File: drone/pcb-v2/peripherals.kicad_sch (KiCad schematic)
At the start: 22 parts, among them J2 Conn_02x11_Odd_Even, J4 Conn_01x04_MountingPin, SW1 SW_Push, SW3 SW_Push, U1 MPU6500, U5 NRF24L01_Breakout, U8 HYCW110-TF10-180B

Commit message: [pcb] schematic v2: footprint/part assignments
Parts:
- C5: renamed from C32; now left out of the parts list
- C6: renamed from C3; footprint Capacitor_SMD:C_0805_2012Metric_Pad1.18x1.45mm_HandSolder -> Capacitor_SMD:C_0603_1608Metric
- C7: renamed from C2; footprint Capacitor_SMD:C_0805_2012Metric_Pad1.18x1.45mm_HandSolder -> Capacitor_SMD:C_0603_1608Metric; LCSC (none) -> C14663
- C8: renamed from C1; footprint Capacitor_SMD:C_0805_2012Metric_Pad1.18x1.45mm_HandSolder -> Capacitor_SMD:C_0603_1608Metric; LCSC (none) -> C14663
- D5: renamed from D7; now left out of the parts list
- D6: renamed from D8; now left out of the parts list
- D7: renamed from D5; now left out of the parts list
- D8: renamed from D6; now left out of the parts list
- J1: renamed from J4; now left out of the parts list
- J2, SW1: now left out of the parts list
- R10: renamed from R23; now left out of the parts list
- R11: renamed from R21; now left out of the parts list
- R12: renamed from R20; now left out of the parts list
- R13: renamed from R22; footprint Resistor_SMD:R_0805_2012Metric -> Resistor_SMD:R_0805_2012Metric_Pad1.20x1.40mm_HandSolder; now left out of the parts list
- R14: renamed from R25; footprint Resistor_SMD:R_0805_2012Metric -> Resistor_SMD:R_0805_2012Metric_Pad1.20x1.40mm_HandSolder; now left out of the parts list
- R9: renamed from R24; now left out of the parts list
- SW2: renamed from SW3; now left out of the parts list
- U1: renamed from U5; now left out of the parts list
- U2: renamed from U8; now left out of the parts list
- renumbered JP2 to JP1, U1 to U3

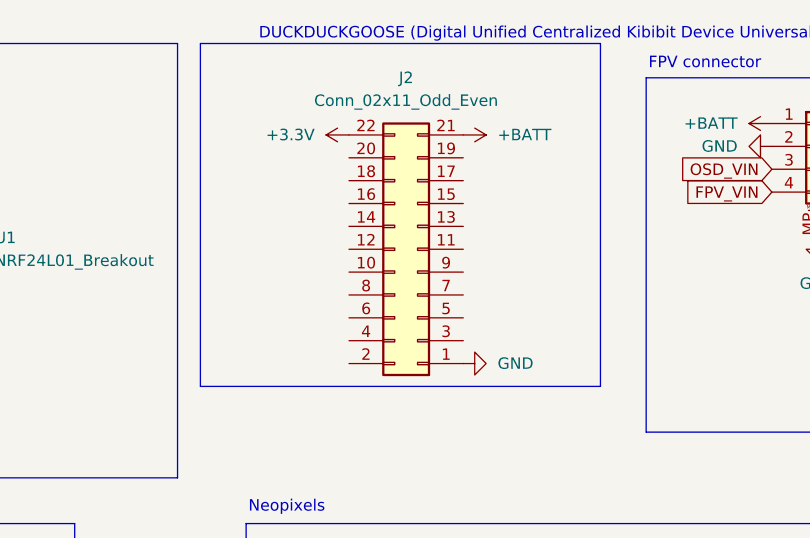
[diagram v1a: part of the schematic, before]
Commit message: [pcb] pcb v2: component placement
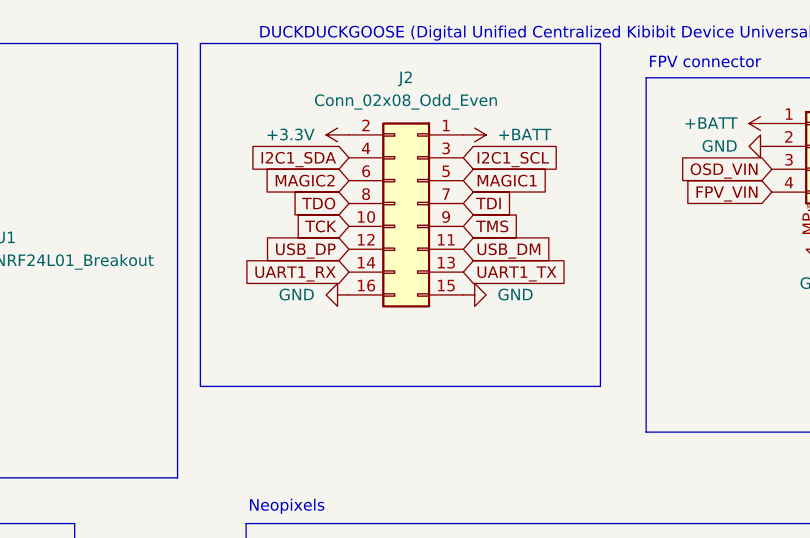
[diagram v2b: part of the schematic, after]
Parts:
- removed J2: Conn_02x11_Odd_Even, Connector_PinHeader_2.54mm:PinHeader_2x11_P2.54mm_Vertical, symbol Connector_Generic:Conn_02x11_Odd_Even
- added J2: Conn_02x08_Odd_Even, Connector_PinHeader_2.54mm:PinHeader_2x08_P2.54mm_Vertical, symbol Connector_Generic:Conn_02x08_Odd_Even
- R10, R11, R12, R9: footprint Resistor_SMD:R_0805_2012Metric_Pad1.20x1.40mm_HandSolder -> Resistor_SMD:R_0805_2012Metric; LCSC (none) -> C17414; now in the parts list
- U3: footprint lcsc:QFN-24_L3.0-W3.0-P0.40-BL-EP -> Package_DFN_QFN:QFN-24-1EP_3x3mm_P0.4mm_EP1.75x1.6mm
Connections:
- net +3.3V: now also J2.2 (Pin_2)
- net +BATT: now also J2.1 (Pin_1)
- net GND: now also J2.15 (Pin_15), J2.16 (Pin_16)
- new net I2C1_SCL: J2.3 (Pin_3)
- new net I2C1_SDA: J2.4 (Pin_4)
- new net MAGIC1: J2.5 (Pin_5)
- new net MAGIC2: J2.6 (Pin_6)
- new net TCK: J2.10 (Pin_10)
- new net TDI: J2.7 (Pin_7)
- new net TDO: J2.8 (Pin_8)
- new net TMS: J2.9 (Pin_9)
- new net UART1_RX: J2.14 (Pin_14)
- new net UART1_TX: J2.13 (Pin_13)
- new net USB_DM: J2.11 (Pin_11)
- new net USB_DP: J2.12 (Pin_12)

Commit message: [pcb] finish routing
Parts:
- removed SW2: SW_Push, lcsc:SW-SMD_L4.0-W2.9-LS5.0, symbol Switch:SW_Push
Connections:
- net SD_CS: no longer U2.9 (CD)
- net SPI1_CLK: no longer U1.5 (SCK)
- net SPI1_MISO: no longer U1.7 (MISO)
- net SPI1_MOSI: no longer U1.6 (MOSI)
- net TCK: now also J2.9 (Pin_9); no longer J2.10 (Pin_10)
- net TMS: now also J2.10 (Pin_10); no longer J2.9 (Pin_9)
- net USB_DM renamed D-
- net USB_DP renamed D+
- new net SD_CD: U2.9 (CD)
- new net SPI2_CLK: U1.5 (SCK)
- new net SPI2_MISO: U1.7 (MISO)
- new net SPI2_MOSI: U1.6 (MOSI)
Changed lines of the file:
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@@
 	(rectangle
 		(start 19.05 69.85)
-		(end 64.77 93.98)
+		(end 40.64 93.98)
 		(stroke
 			(width 0)
@@
 		)
 	)
-	(global_label "SPI1_MOSI"
+	(global_label "SPI2_MOSI"
 		(shape input)
 		(at 33.02 31.75 180)
@@
 		)
 	)
-	(global_label "USB_DP"
+	(global_label "D-"
 		(shape input)
-		(at 95.25 39.37 180)
+		(at 107.95 39.37 0)
 		(fields_autoplaced yes)
 		(effects
@@
 				(size 1.27 1.27)
 			)
-			(justify right)
+			(justify left)
 		)
 		(property "Intersheetrefs" "${INTERSHEET_REFS}"
-			(at 84.9472 39.37 0)
+			(at 113.7776 39.37 0)
 			(effects
 				(font
 					(size 1.27 1.27)
 				)
-				(justify right)
+				(justify left)
 				(hide yes)
 			)
@@
 		)
 	)
-	(global_label "BTN2"
+	(global_label "IMU_INT1"
 		(shape input)
-		(at 54.61 85.09 0)
+		(at 41.91 137.16 180)
 		(fields_autoplaced yes)
 		(effects
@@
 				(size 1.27 1.27)
 			)
-			(justify left)
+			(justify right)
 		)
 		(property "Intersheetrefs" "${INTERSHEET_REFS}"
-			(at 62.3728 85.09 0)
+			(at 30.4581 137.16 0)
 			(effects
 				(font
 					(size 1.27 1.27)
 				)
-				(justify left)
+				(justify right)
 				(hide yes)
 			)
 		)
 	)
-	(global_label "TMS"
+	(global_label "BTN1"
 		(shape input)
-		(at 107.95 36.83 0)
+		(at 31.75 85.09 0)
 		(fields_autoplaced yes)
 		(effects
@@
 		)
 		(property "Intersheetrefs" "${INTERSHEET_REFS}"
-			(at 114.5637 36.83 0)
+			(at 39.5128 85.09 0)
 			(effects
 				(font
@@
 		)
 	)
-	(global_label "IMU_INT1"
+	(global_label "SPI1_CLK"
 		(shape input)
-		(at 41.91 137.16 180)
+		(at 236.22 49.53 180)
 		(fields_autoplaced yes)
 		(effects
@@
 		)
 		(property "Intersheetrefs" "${INTERSHEET_REFS}"
-			(at 30.4581 137.16 0)
+			(at 224.4053 49.53 0)
 			(effects
 				(font
@@
 		)
 	)
-	(global_label "BTN1"
-		(shape input)
-		(at 31.75 85.09 0)
-		(fields_autoplaced yes)
-		(effects
-			(font
-				(size 1.27 1.27)
-			)
-			(justify left)
-		)
-		(property "Intersheetrefs" "${INTERSHEET_REFS}"
-			(at 39.5128 85.09 0)
-			(effects
-				(font
-					(size 1.27 1.27)
-				)
-				(justify left)
-				(hide yes)
-			)
-		)
-	)
-	(global_label "SPI1_CLK"
+	(global_label "MAGIC2"
 		(shape input)
-		(at 236.22 49.53 180)
+		(at 95.25 31.75 180)
 		(fields_autoplaced yes)
 		(effects
@@
 		)
 		(property "Intersheetrefs" "${INTERSHEET_REFS}"
-			(at 224.4053 49.53 0)
+			(at 85.3705 31.75 0)
 			(effects
 				(font
@@
 		)
 	)
-	(global_label "USB_DM"
+	(global_label "STATUS_LED_2"
 		(shape input)
-		(at 107.95 39.37 0)
+		(at 190.5 116.84 0)
 		(fields_autoplaced yes)
 		(effects
@@
 		)
 		(property "Intersheetrefs" "${INTERSHEET_REFS}"
-			(at 118.4342 39.37 0)
+			(at 206.8503 116.84 0)
 			(effects
 				(font
@@
 		)
 	)
-	(global_label "MAGIC2"
+	(global_label "TCK"
 		(shape input)
-		(at 95.25 31.75 180)
+		(at 107.95 36.83 0)
 		(fields_autoplaced yes)
 		(effects
@@
 				(size 1.27 1.27)
 			)
-			(justify right)
+			(justify left)
 		)
 		(property "Intersheetrefs" "${INTERSHEET_REFS}"
-			(at 85.3705 31.75 0)
+			(at 114.4428 36.83 0)
 			(effects
 				(font
 					(size 1.27 1.27)
 				)
-				(justify right)
+				(justify left)
 				(hide yes)
 			)
 		)
 	)
-	(global_label "STATUS_LED_2"
+	(global_label "D+"
 		(shape input)
-		(at 190.5 116.84 0)
+		(at 95.25 39.37 180)
 		(fields_autoplaced yes)
 		(effects
@@
 				(size 1.27 1.27)
 			)
-			(justify left)
+			(justify right)
 		)
 		(property "Intersheetrefs" "${INTERSHEET_REFS}"
-			(at 206.8503 116.84 0)
+			(at 89.4224 39.37 0)
 			(effects
 				(font
 					(size 1.27 1.27)
 				)
-				(justify left)
+				(justify right)
 				(hide yes)
 			)
@@
 		)
 	)
-	(global_label "SPI1_CLK"
+	(global_label "SPI2_CLK"
 		(shape input)
 		(at 33.02 36.83 180)
@@
 		)
 	)
-	(global_label "SPI1_MISO"
+	(global_label "SPI2_MISO"
 		(shape input)
 		(at 33.02 34.29 180)
@@
 		)
 	)
-	(global_label "SPI1_MISO"
+	(global_label "TMS"
 		(shape input)
-		(at 41.91 129.54 180)
+		(at 95.25 36.83 180)
 		(fields_autoplaced yes)
 		(effects
@@
 		)
 		(property "Intersheetrefs" "${INTERSHEET_REFS}"
-			(at 29.0672 129.54 0)
+			(at 88.6363 36.83 0)
 			(effects
 				(font
@@
 		)
 	)
-	(global_label "SD_CS"
+	(global_label "SPI1_MISO"
 		(shape input)
-		(at 256.54 44.45 0)
+		(at 41.91 129.54 180)
 		(fields_autoplaced yes)
 		(effects
@@
 				(size 1.27 1.27)
 			)
-			(justify left)
+			(justify right)
 		)
 		(property "Intersheetrefs" "${INTERSHEET_REFS}"
-			(at 265.4518 44.45 0)
+			(at 29.0672 129.54 0)
 			(effects
 				(font
 					(size 1.27 1.27)
 				)
-				(justify left)
+				(justify right)
 				(hide yes)
 			)
 		)
 	)
-	(global_label "MAGIC1"
+	(global_label "SD_CD"
 		(shape input)
-		(at 107.95 31.75 0)
+		(at 256.54 44.45 0)
 		(fields_autoplaced yes)
 		(effects
@@
 		)
 		(property "Intersheetrefs" "${INTERSHEET_REFS}"
-			(at 117.8295 31.75 0)
+			(at 265.5123 44.45 0)
 			(effects
 				(font
@@
 		)
 	)
-	(global_label "TCK"
+	(global_label "MAGIC1"
 		(shape input)
-		(at 95.25 36.83 180)
+		(at 107.95 31.75 0)
 		(fields_autoplaced yes)
 		(effects
@@
 				(size 1.27 1.27)
 			)
-			(justify right)
+			(justify left)
 		)
 		(property "Intersheetrefs" "${INTERSHEET_REFS}"
-			(at 88.7572 36.83 0)
+			(at 117.8295 31.75 0)
 			(effects
 				(font
 					(size 1.27 1.27)
 				)
-				(justify right)
+				(justify left)
 				(hide yes)
 			)
@@
 	)
 	(symbol
-		(lib_id "Switch:SW_Push")
-		(at 49.53 85.09 0)
-		(unit 1)
-		(exclude_from_sim no)
-		(in_bom no)
-		(on_board yes)
-		(dnp no)
-		(fields_autoplaced yes)
-		(property "Reference" "SW2"
-			(at 49.53 77.47 0)
-			(effects
-				(font
-					(size 1.27 1.27)
-				)
-			)
-		)
-		(property "Value" "SW_Push"
-			(at 49.53 80.01 0)
-			(effects
-				(font
-					(size 1.27 1.27)
-				)
-			)
-		)
-		(property "Footprint" "lcsc:SW-SMD_L4.0-W2.9-LS5.0"
-			(at 49.53 80.01 0)
-			(effects
-				(font
-					(size 1.27 1.27)
-				)
-				(hide yes)
-			)
-		)
-		(property "Datasheet" "~"
-			(at 49.53 80.01 0)
-			(effects
-				(font
-					(size 1.27 1.27)
-				)
-				(hide yes)
-			)
-		)
-		(property "Description" "Push button switch, generic, two pins"
-			(at 49.53 85.09 0)
-			(effects
-				(font
-					(size 1.27 1.27)
-				)
-				(hide yes)
-			)
-		)
-		(pin "1"
-		)
-		(pin "2"
-		)
-		(instances
-			(project "astra"
-				(path "/c0be3de2-9de4-4447-aa6f-537ea5f31aac/5121fc52-65c9-43af-86a0-4c1ef24f194e"
-					(reference "SW3")
-					(unit 1)
-				)
-			)
-			(project "astra"
-				(path "/e7184c3b-9f46-4a4e-9d8d-c6d386a497ae/2b0c3b06-bbfe-4747-abd1-836d8053a37d"
-					(reference "SW2")
-					(unit 1)
-				)
-			)
-		)
-	)
-	(symbol
 		(lib_id "LED:WS2812B")
 		(at 106.68 83.82 0)
@@
 					(unit 1)
 				)
-			)
-		)
-	)
-	(symbol
-		(lib_id "power:GND")
-		(at 44.45 85.09 0)
-		(unit 1)
-		(exclude_from_sim no)
-		(in_bom yes)
-		(on_board yes)
-		(dnp no)
-		(fields_autoplaced yes)
-		(property "Reference" "#PWR024"
-			(at 44.45 91.44 0)
-			(effects
-				(font
-					(size 1.27 1.27)
-				)
-				(hide yes)
-			)
-		)
-		(property "Value" "GND"
-			(at 44.45 90.17 0)
-			(effects
-				(font
-					(size 1.27 1.27)
-				)
-			)
-		)
-		(property "Footprint" ""
-			(at 44.45 85.09 0)
-			(effects
-				(font
-					(size 1.27 1.27)
-				)
-				(hide yes)
-			)
-		)
-		(property "Datasheet" ""
-			(at 44.45 85.09 0)
-			(effects
-				(font
-					(size 1.27 1.27)
-				)
-				(hide yes)
-			)
-		)
-		(property "Description" "Power symbol creates a global label with name \"GND\" , ground"
-			(at 44.45 85.09 0)
-			(effects
-				(font
-					(size 1.27 1.27)
-				)
-				(hide yes)
-			)
-		)
-		(pin "1"
-		)
-		(instances
-			(project ""
-				(path "/c0be3de2-9de4-4447-aa6f-537ea5f31aac/5121fc52-65c9-43af-86a0-4c1ef24f194e"
-					(reference "#PWR041")
-					(unit 1)
-				)
-			)
-			(project ""
-				(path "/e7184c3b-9f46-4a4e-9d8d-c6d386a497ae/2b0c3b06-bbfe-4747-abd1-836d8053a37d"
-					(reference "#PWR024")
-					(unit 1)
-				)
